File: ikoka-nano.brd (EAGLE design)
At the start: 22.5 x 33 mm, 6 parts, among them IC1 E22-900M22S, J1 Vertical Qwiic Connector, J2 Vertical Qwiic Connector, J3 Vertical Qwiic Connector

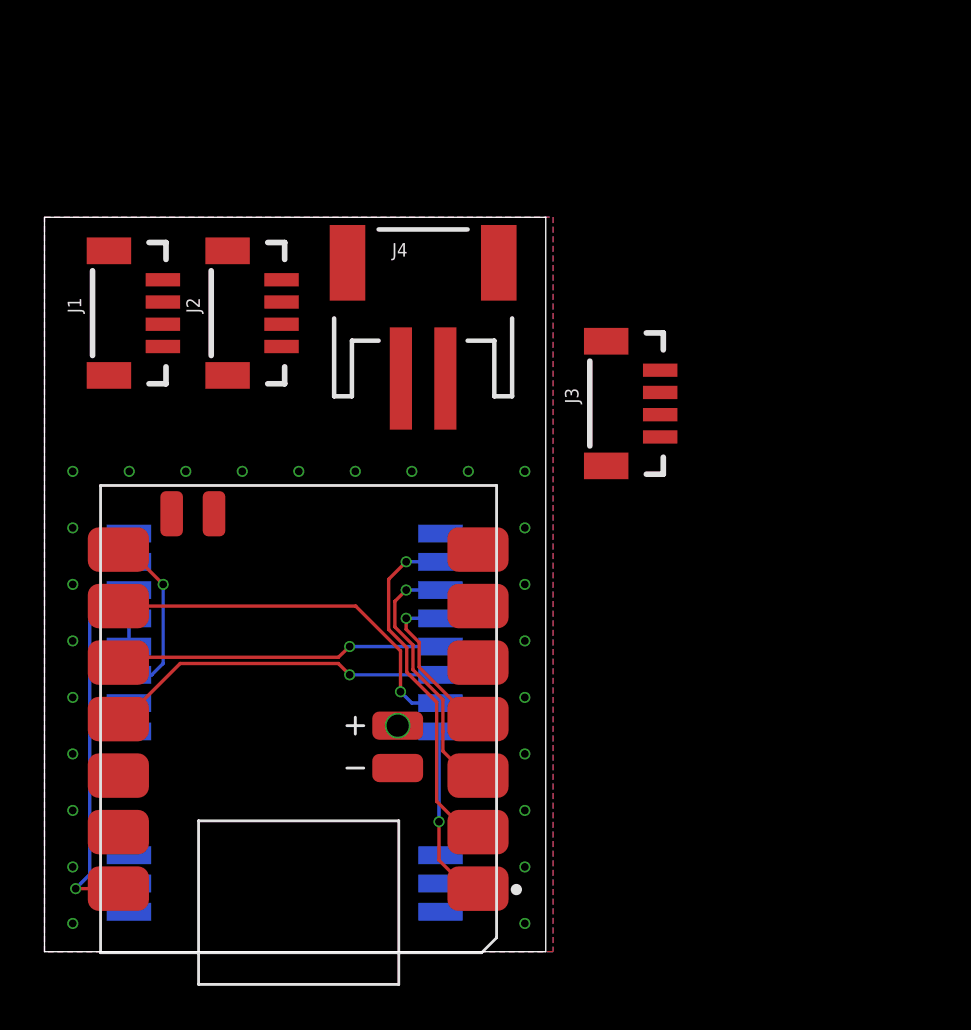
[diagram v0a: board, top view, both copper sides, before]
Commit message: Redesign board because the E22-900M22S footprint from SnapMagic was much smaller than the actual module size; add solar 5V connector; reduce Qwiic connectors to just one.
Signed-off-by: Andrew Yong <me@ndoo.sg>
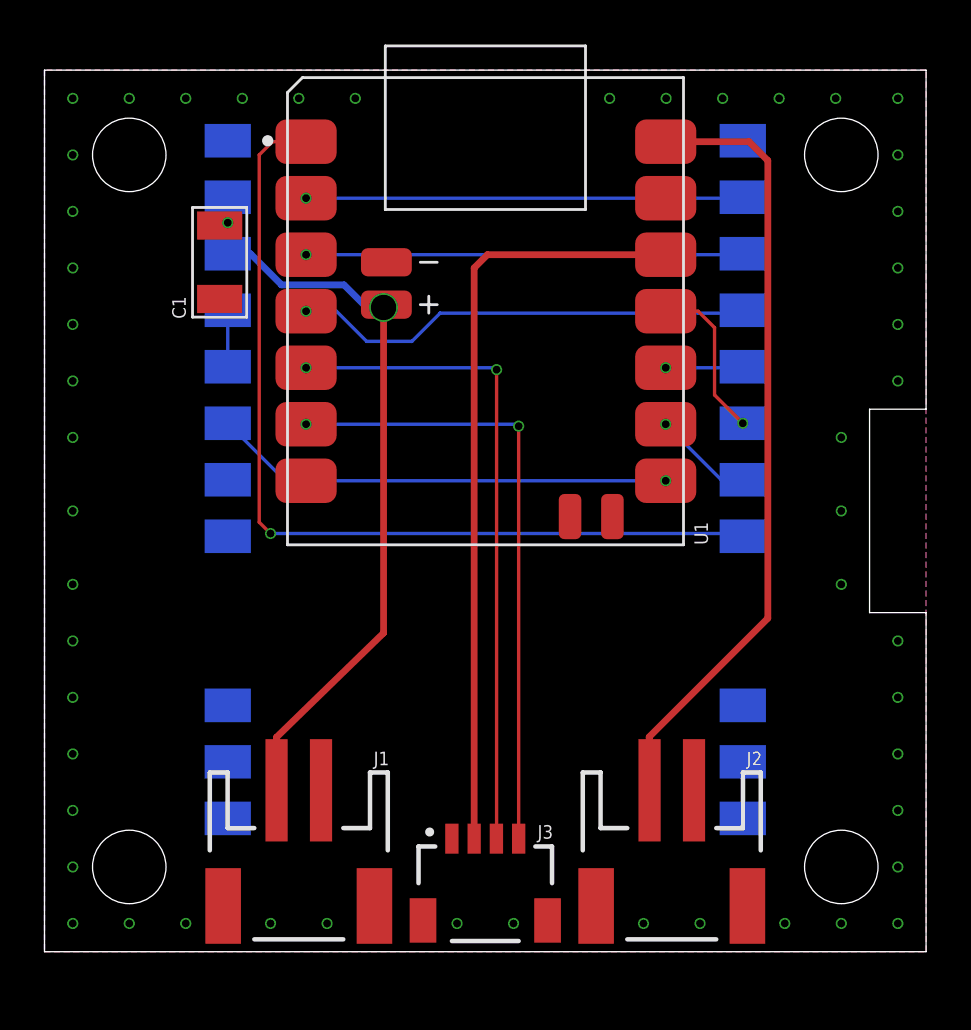
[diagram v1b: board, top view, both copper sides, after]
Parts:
- removed IC1: E22-900M22S, E22-900M22S:E22-900M22S
- removed J4: (no value), SparkFun-Connectors:JST-2-SMD
- added C1: 100uf, OPL_Capacitor:C1206
- added H1, H2, H3, H4: STAND-OFF, SparkFun-Hardware:STAND-OFF
- added U2: E22-900M30S, E22-900M30S:XCVR_E22-900M30S
- J1: value Vertical Qwiic Connector -> LiPo 1S; device SparkFun-Connectors:JST04_1MM_VERT -> SparkFun-Connectors:JST-2-SMD
- J2: value Vertical Qwiic Connector -> Solar ≤6.45V; device SparkFun-Connectors:JST04_1MM_VERT -> SparkFun-Connectors:JST-2-SMD
- J3: value Vertical Qwiic Connector -> Qwiic; device SparkFun-Connectors:JST04_1MM_VERT -> SparkFun-Connectors:JST04_1MM_RA
- U1: value (none) -> XIAO BLE nRF52840
- moved J2 30.2 mm to (28.2, 3.56), turned to 180 degrees
- moved J1 25.7 mm to (11.4, 3.56), turned to 180 degrees
- moved J3 21.4 mm to (19.8, 5.08), turned to 0 degrees
- moved U1 7.51 mm to (19.8, 28.4), turned to 0 degrees
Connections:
- removed net I2C_SDL: U1.6
- removed net N$24: IC1.21
- removed net SX126X_TXEN: IC1.7, IC1.8
- new net SX126X_TXEN/DIO2: U2.7, U2.8
- net 3V3: no longer J1.2, J2.2
- net 5V: now also J2.2; no longer IC1.9
- net GND: now also C1.2, U2.1, U2.11, U2.12, U2.2, U2.20, U2.22, U2.3, U2.4, U2.5; no longer IC1.1, IC1.10, IC1.11, IC1.12, IC1.2, IC1.20, IC1.22, IC1.3, IC1.4, IC1.5, J4.1
- net I2C_SCL: now also U1.6; no longer J1.4, J2.4
- net I2C_SDA: no longer J1.3, J2.3
- net SPI_MISO: now also U2.16; no longer IC1.16
- net SPI_MOSI: now also U2.17; no longer IC1.17
- net SPI_SCK: now also U2.18; no longer IC1.18
- net SX126X_BUSY: now also U2.14; no longer IC1.14
- net SX126X_CS: now also U2.19; no longer IC1.19
- net SX126X_DIO1: now also U2.13; no longer IC1.13
- net SX126X_RESET: now also U2.15; no longer IC1.15
- net SX126X_RXEN: now also U2.6; no longer IC1.6
- net VBAT: now also C1.1, J1.2, U2.10, U2.9; no longer J4.2
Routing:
- net VBAT: track 0.00 -> 34.9 mm, vias 1 -> 2
- net 3V3: track 0.00 -> 34.5 mm
- net SX126X_CS: track 8.10 -> 40.9 mm
- net I2C_SDA: track 0.00 -> 29.7 mm, vias 0 -> 2
- net I2C_SCL: track 0.00 -> 28.2 mm, vias 0 -> 2
- net 5V: track 17.1 -> 35.5 mm, vias 1 -> 0
- net SX126X_RESET: track 7.59 -> 20.8 mm
- net SPI_SCK: track 17.4 -> 4.50 mm
- net SX126X_RXEN: track 7.97 -> 20.8 mm
- net SPI_MISO: track 14.8 -> 3.51 mm
- net SPI_MOSI: track 15.7 -> 7.32 mm
- net SX126X_BUSY: track 11.9 -> 19.6 mm
- net SX126X_DIO1: track 16.0 -> 19.7 mm
- net SX126X_TXEN/DIO2: track 0.00 -> 2.54 mm
- net SX126X_TXEN: track 1.27 -> 0.00 mm
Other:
- board size 22.5 x 33 mm -> 39.6 x 39.6 mm
- board text added: "Qwiic"
